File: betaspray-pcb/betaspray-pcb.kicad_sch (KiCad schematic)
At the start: 11 parts, among them SW1 SW_Push, SW2 SW_Push, U1 ESP32-S3-WROOM-1

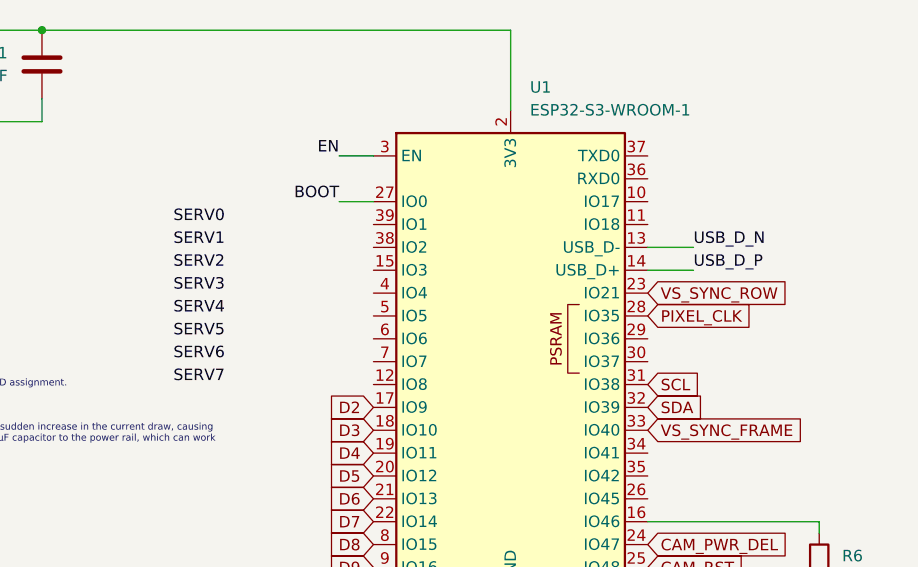
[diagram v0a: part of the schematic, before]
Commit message: fix servo pins
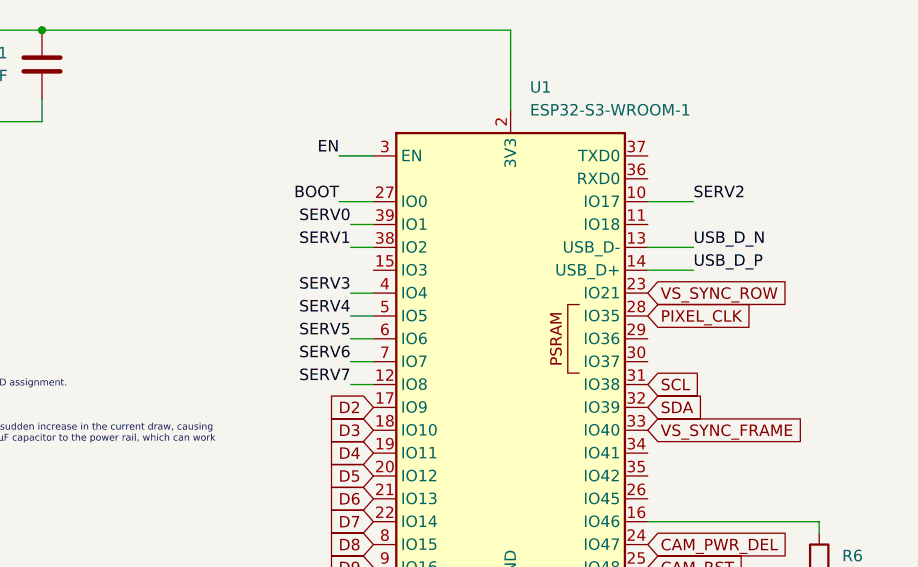
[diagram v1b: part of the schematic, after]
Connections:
- net SERV0: now also U1.39 (IO1)
- net SERV1: now also U1.38 (IO2)
- net SERV2: now also U1.10 (IO17)
- net SERV3: now also U1.4 (IO4)
- net SERV4: now also U1.5 (IO5)
- net SERV5: now also U1.6 (IO6)
- net SERV6: now also U1.7 (IO7)
- net SERV7: now also U1.12 (IO8)
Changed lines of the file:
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@@
+	(wire
+		(pts
+			(xy 93.98 63.5) (xy 96.52 63.5)
+		)
+		(stroke
+			(width 0)
+			(type default)
+		)
+	)
 	(wire
 		(pts
@@
 	(wire
 		(pts
+			(xy 93.98 53.34) (xy 96.52 53.34)
+		)
+		(stroke
+			(width 0)
+			(type default)
+		)
+	)
+	(wire
+		(pts
 			(xy 146.05 92.71) (xy 146.05 93.98)
 		)
@@
 	(wire
 		(pts
+			(xy 93.98 60.96) (xy 96.52 60.96)
+		)
+		(stroke
+			(width 0)
+			(type default)
+		)
+	)
+	(wire
+		(pts
 			(xy 111.76 29.21) (xy 111.76 38.1)
 		)
@@
 	(wire
 		(pts
+			(xy 127 48.26) (xy 132.08 48.26)
+		)
+		(stroke
+			(width 0)
+			(type default)
+		)
+	)
+	(wire
+		(pts
 			(xy 186.69 62.23) (xy 186.69 63.5)
 		)
@@
 	(wire
 		(pts
+			(xy 93.98 68.58) (xy 96.52 68.58)
+		)
+		(stroke
+			(width 0)
+			(type default)
+		)
+	)
+	(wire
+		(pts
 			(xy 146.05 85.09) (xy 146.05 83.82)
 		)
@@
 	(wire
 		(pts
+			(xy 93.98 58.42) (xy 96.52 58.42)
+		)
+		(stroke
+			(width 0)
+			(type default)
+		)
+	)
+	(wire
+		(pts
 			(xy 92.71 48.26) (xy 96.52 48.26)
 		)
@@
 	(wire
 		(pts
+			(xy 93.98 50.8) (xy 96.52 50.8)
+		)
+		(stroke
+			(width 0)
+			(type default)
+		)
+	)
+	(wire
+		(pts
 			(xy 186.69 59.69) (xy 186.69 62.23)
 		)
@@
 		(pts
 			(xy 278.13 11.43) (xy 278.13 82.55)
+		)
+		(stroke
+			(width 0)
+			(type default)
+		)
+	)
+	(wire
+		(pts
+			(xy 93.98 66.04) (xy 96.52 66.04)
 		)
 		(stroke
@@
 	)
 	(label "SERV1"
-		(at 80.01 53.34 180)
+		(at 93.98 53.34 180)
 		(effects
 			(font
@@
 	)
 	(label "SERV0"
-		(at 80.01 50.8 180)
+		(at 93.98 50.8 180)
 		(effects
 			(font
@@
 	)
 	(label "SERV3"
-		(at 80.01 58.42 180)
+		(at 93.98 58.42 180)
 		(effects
 			(font
@@
 	)
 	(label "SERV7"
-		(at 80.01 68.58 180)
+		(at 93.98 68.58 180)
 		(effects
 			(font
@@
 	)
 	(label "SERV6"
-		(at 80.01 66.04 180)
+		(at 93.98 66.04 180)
 		(effects
 			(font
@@
 	)
 	(label "SERV4"
-		(at 80.01 60.96 180)
+		(at 93.98 60.96 180)
 		(effects
 			(font
@@
 	)
 	(label "SERV2"
-		(at 80.01 55.88 180)
-		(effects
-			(font
-				(size 1.27 1.27)
-			)
-			(justify right bottom)
+		(at 132.08 48.26 0)
+		(effects
+			(font
+				(size 1.27 1.27)
+			)
+			(justify left bottom)
 		)
 	)
@@
 	)
 	(label "SERV5"
-		(at 80.01 63.5 180)
-		(effects
-			(font
+		(at 93.98 63.5 180)
+		(effects
+			(font

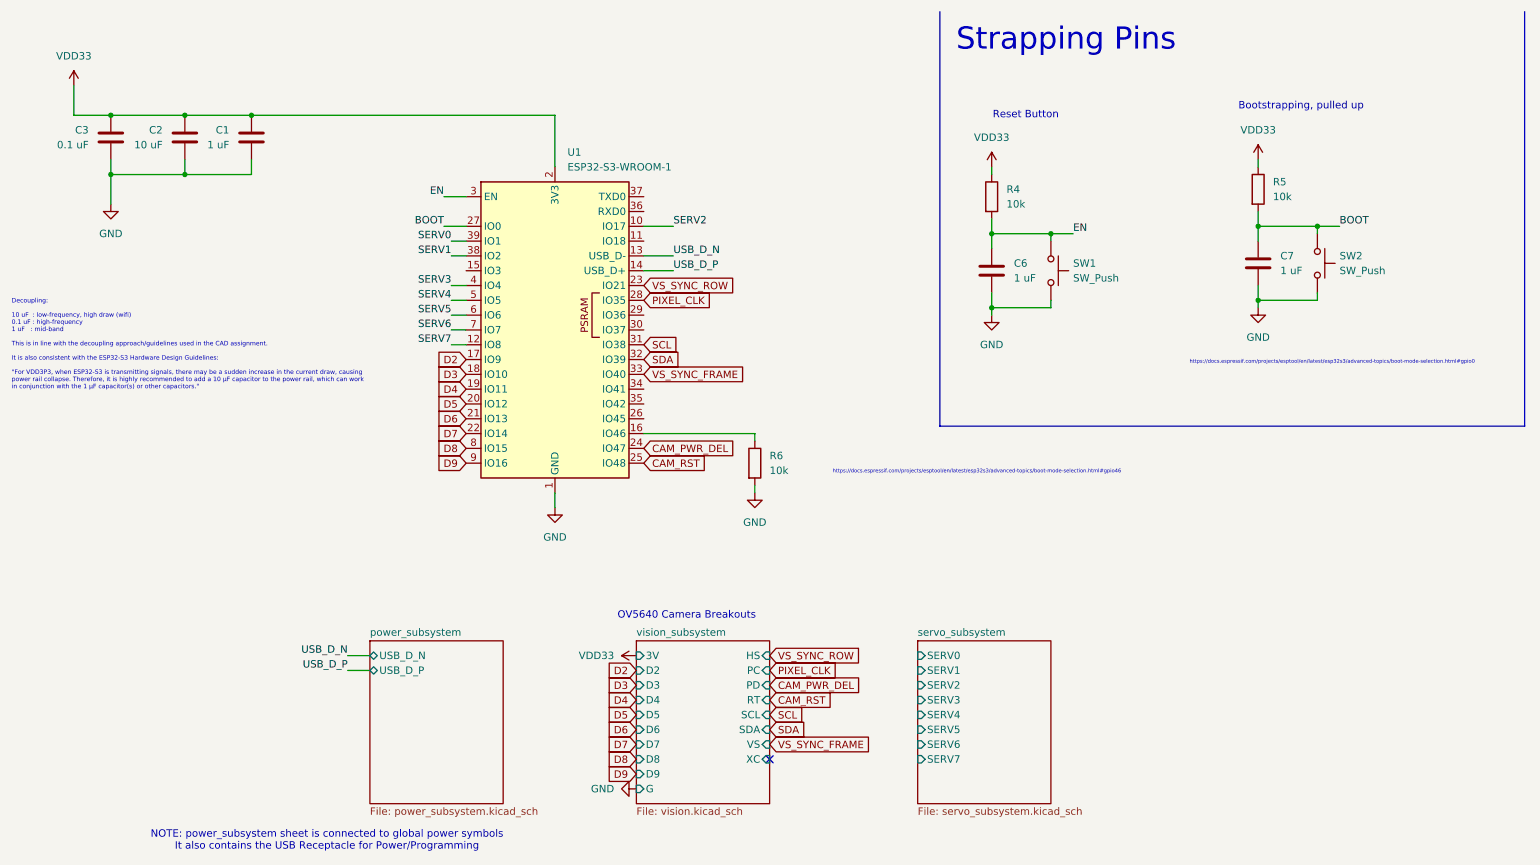
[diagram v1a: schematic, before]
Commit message: Connected Servo labels, added debug led
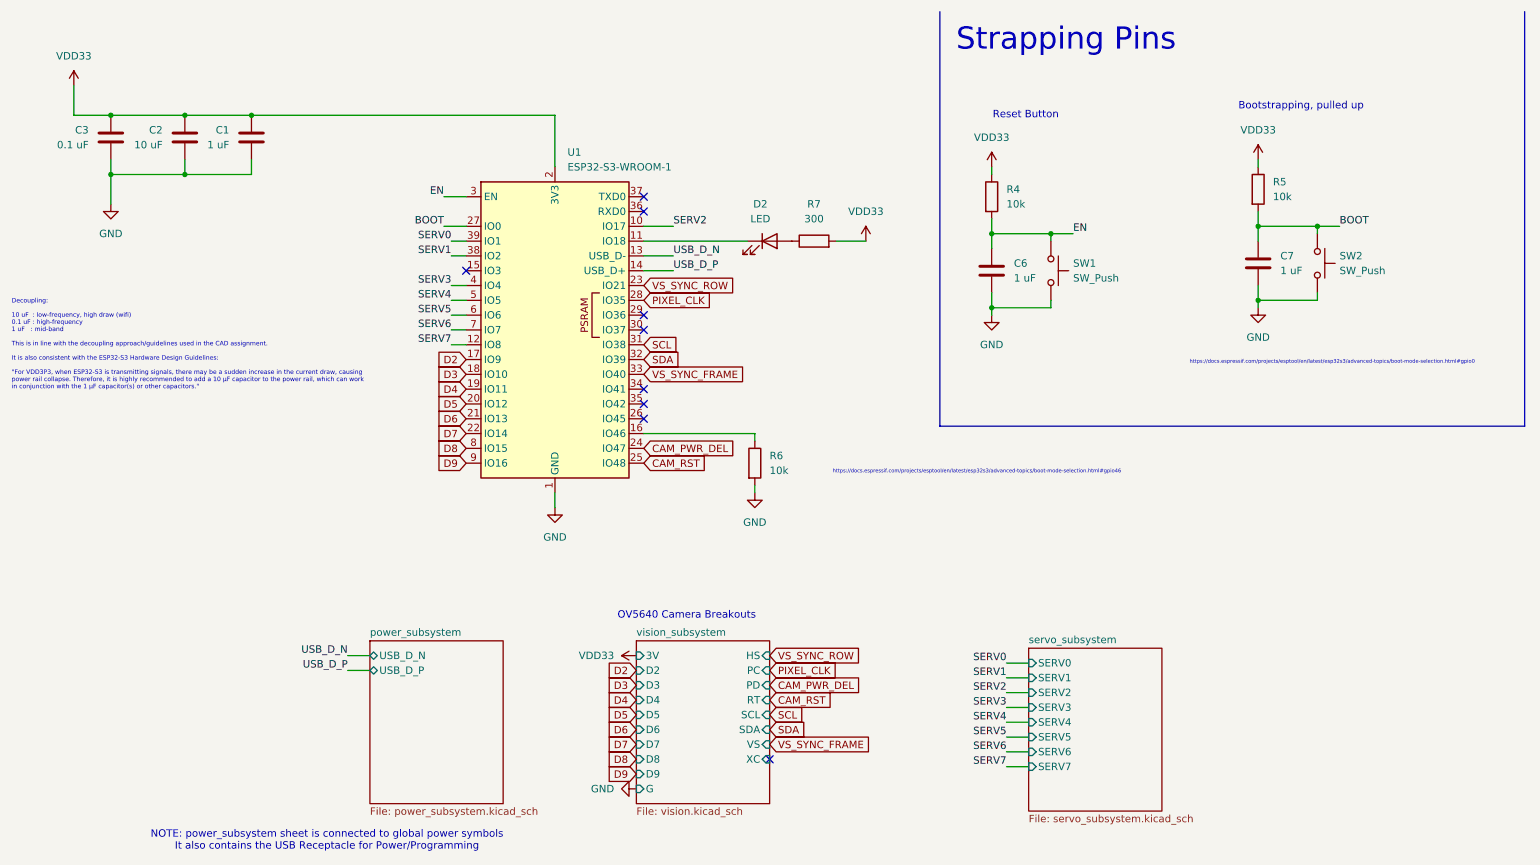
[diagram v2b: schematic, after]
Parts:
- added D2: LED, LED_SMD:LED_0805_2012Metric, symbol betaspray_MCU_Espressif:LED
- added R7: 300, symbol betaspray_MCU_Espressif:R
- C1, C2, C6, C7: symbol betaspray_LDO:C -> betaspray_MCU_Espressif:C
- C3: symbol Device:C -> betaspray_MCU_Espressif:C
- R4, R5, R6: symbol betaspray_LDO:R -> betaspray_MCU_Espressif:R
- SW1, SW2: symbol betaspray_LDO:SW_Push -> betaspray_MCU_Espressif:SW_Push
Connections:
- net VDD33: now also R7.2
- net at U1.11 (IO18): now also D2.1 (K)
- new net: D2.2 (A), R7.1
- no-connect marks 1 -> 9

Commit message: Started layout
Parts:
- C1, C2, C3, C6, C7: footprint (none) -> Capacitor_SMD:C_0805_2012Metric_Pad1.18x1.45mm_HandSolder
- R4, R5, R6, R7: footprint (none) -> Resistor_SMD:R_0805_2012Metric_Pad1.20x1.40mm_HandSolder
- SW1, SW2: footprint (none) -> Button_Switch_THT:SW_PUSH-12mm
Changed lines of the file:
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@@
 			)
 		)
-		(property "Footprint" ""
+		(property "Footprint" "Capacitor_SMD:C_0805_2012Metric_Pad1.18x1.45mm_HandSolder"
 			(at 34.5948 36.83 0)
 			(effects
@@
 			)
 		)
-		(property "Footprint" ""
+		(property "Footprint" "Button_Switch_THT:SW_PUSH-12mm"
 			(at 247.65 54.61 0)
 			(effects
@@
 			)
 		)
-		(property "Footprint" ""
+		(property "Footprint" "Resistor_SMD:R_0805_2012Metric_Pad1.20x1.40mm_HandSolder"
 			(at 156.21 52.578 90)
 			(effects
@@
 			)
 		)
-		(property "Footprint" ""
+		(property "Footprint" "Resistor_SMD:R_0805_2012Metric_Pad1.20x1.40mm_HandSolder"
 			(at 184.912 43.18 90)
 			(effects
@@
 			)
 		)
-		(property "Footprint" ""
+		(property "Footprint" "Capacitor_SMD:C_0805_2012Metric_Pad1.18x1.45mm_HandSolder"
 			(at 187.6552 59.69 0)
 			(effects
@@
 			)
 		)
-		(property "Footprint" ""
+		(property "Footprint" "Button_Switch_THT:SW_PUSH-12mm"
 			(at 201.93 55.88 0)
 			(effects
@@
 			)
 		)
-		(property "Footprint" ""
+		(property "Footprint" "Capacitor_SMD:C_0805_2012Metric_Pad1.18x1.45mm_HandSolder"
 			(at 233.3752 58.42 0)
 			(effects
@@
 			)
 		)
-		(property "Footprint" ""
+		(property "Footprint" "Resistor_SMD:R_0805_2012Metric_Pad1.20x1.40mm_HandSolder"
 			(at 144.272 88.9 90)
 			(effects
@@
 			)
 		)
-		(property "Footprint" ""
+		(property "Footprint" "Resistor_SMD:R_0805_2012Metric_Pad1.20x1.40mm_HandSolder"
 			(at 230.632 41.91 90)
 			(effects
@@
 			)
 		)
-		(property "Footprint" ""
+		(property "Footprint" "Capacitor_SMD:C_0805_2012Metric_Pad1.18x1.45mm_HandSolder"
 			(at 47.2948 36.83 0)
 			(effects
@@
 			)
 		)
-		(property "Footprint" ""
+		(property "Footprint" "Capacitor_SMD:C_0805_2012Metric_Pad1.18x1.45mm_HandSolder"
 			(at 58.7248 36.83 0)
 			(effects

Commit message: Trying to route
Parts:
- SW1, SW2: footprint Button_Switch_THT:SW_PUSH-12mm -> Button_Switch_SMD:SW_DIP_SPSTx02_Slide_9.78x7.26mm_W8.61mm_P2.54mm
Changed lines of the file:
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@@
 			)
 		)
-		(property "Footprint" "Button_Switch_THT:SW_PUSH-12mm"
+		(property "Footprint" "Button_Switch_SMD:SW_DIP_SPSTx02_Slide_9.78x7.26mm_W8.61mm_P2.54mm"
 			(at 247.65 54.61 0)
 			(effects
@@
 			)
 		)
-		(property "Footprint" "Button_Switch_THT:SW_PUSH-12mm"
+		(property "Footprint" "Button_Switch_SMD:SW_DIP_SPSTx02_Slide_9.78x7.26mm_W8.61mm_P2.54mm"
 			(at 201.93 55.88 0)
 			(effects

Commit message: Trying to route
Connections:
- net CAM_PWR_DEL: now also U1.28 (IO35); no longer U1.24 (IO47)
- net D2: now also U1.24 (IO47); no longer U1.17 (IO9)
- net D3: now also U1.23 (IO21); no longer U1.18 (IO10)
- net PIXEL_CLK: now also U1.39 (IO1); no longer U1.28 (IO35)
- net SCL: now also U1.33 (IO40); no longer U1.31 (IO38)
- net SERV0: now also U1.4 (IO4); no longer U1.39 (IO1)
- net SERV1: now also U1.5 (IO5); no longer U1.38 (IO2)
- net SERV3: now also U1.17 (IO9); no longer U1.4 (IO4)
- net SERV4: now also U1.6 (IO6); no longer U1.5 (IO5)
- net SERV5: now also U1.12 (IO8); no longer U1.6 (IO6)
- net SERV7: now also U1.18 (IO10); no longer U1.12 (IO8)
- net VS_SYNC_FRAME: now also U1.31 (IO38); no longer U1.33 (IO40)
- net VS_SYNC_ROW: now also U1.38 (IO2); no longer U1.23 (IO21)
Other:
- sheet power_subsystem ports: added VDD3V; removed none

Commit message: Routed
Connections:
- net CAM_PWR_DEL: now also U1.19 (IO11); no longer U1.28 (IO35)
- net CAM_RST: now also U1.26 (IO45); no longer U1.25 (IO48)
- net D2: now also U1.20 (IO12); no longer U1.24 (IO47)
- net D3: now also U1.31 (IO38); no longer U1.23 (IO21)
- net D4: now also U1.21 (IO13); no longer U1.19 (IO11)
- net D5: now also U1.32 (IO39); no longer U1.20 (IO12)
- net D6: now also U1.22 (IO14); no longer U1.21 (IO13)
- net D7: now also U1.33 (IO40); no longer U1.22 (IO14)
- net D8: now also U1.23 (IO21); no longer U1.8 (IO15)
- net D9: now also U1.34 (IO41); no longer U1.9 (IO16)
- net PIXEL_CLK: now also U1.35 (IO42); no longer U1.39 (IO1)
- net SCL: now also U1.39 (IO1); no longer U1.33 (IO40)
- net SDA: now also U1.25 (IO48); no longer U1.32 (IO39)
- net SERV1: now also U1.6 (IO6); no longer U1.5 (IO5)
- net SERV2: now also U1.11 (IO18); no longer U1.10 (IO17)
- net SERV3: now also U1.12 (IO8); no longer U1.17 (IO9)
- net SERV4: now also U1.17 (IO9); no longer U1.6 (IO6)
- net SERV5: now also U1.5 (IO5); no longer U1.12 (IO8)
- net VS_SYNC_FRAME: now also U1.38 (IO2); no longer U1.31 (IO38)
- net VS_SYNC_ROW: now also U1.24 (IO47); no longer U1.38 (IO2)
- net at D2.1 (K): now also U1.10 (IO17); no longer U1.11 (IO18)
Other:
- moved on the sheet: D2, R7

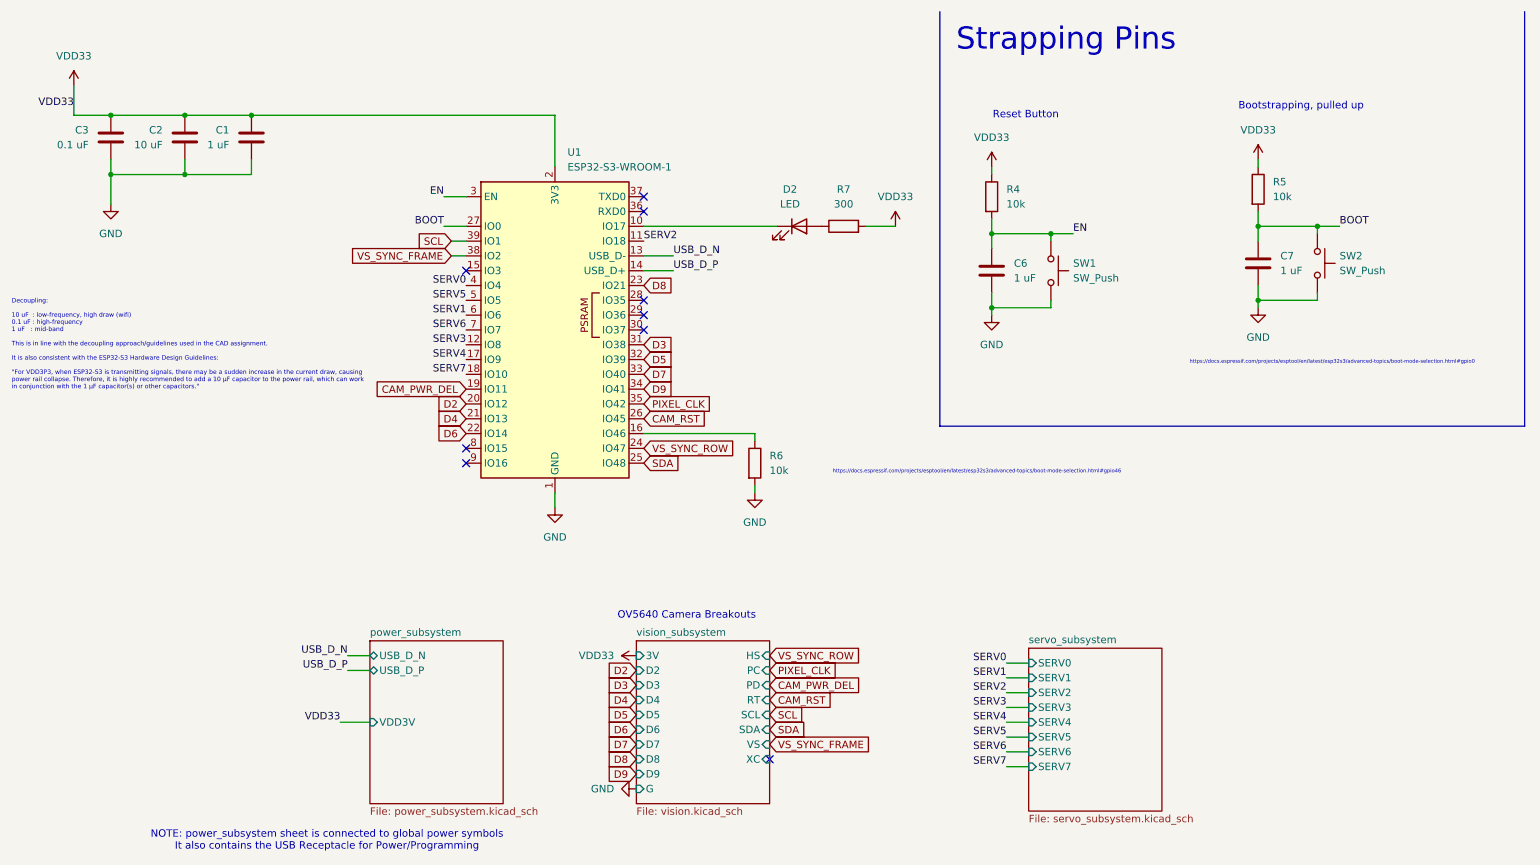
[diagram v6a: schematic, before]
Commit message: Added lasers to schematic and footprint
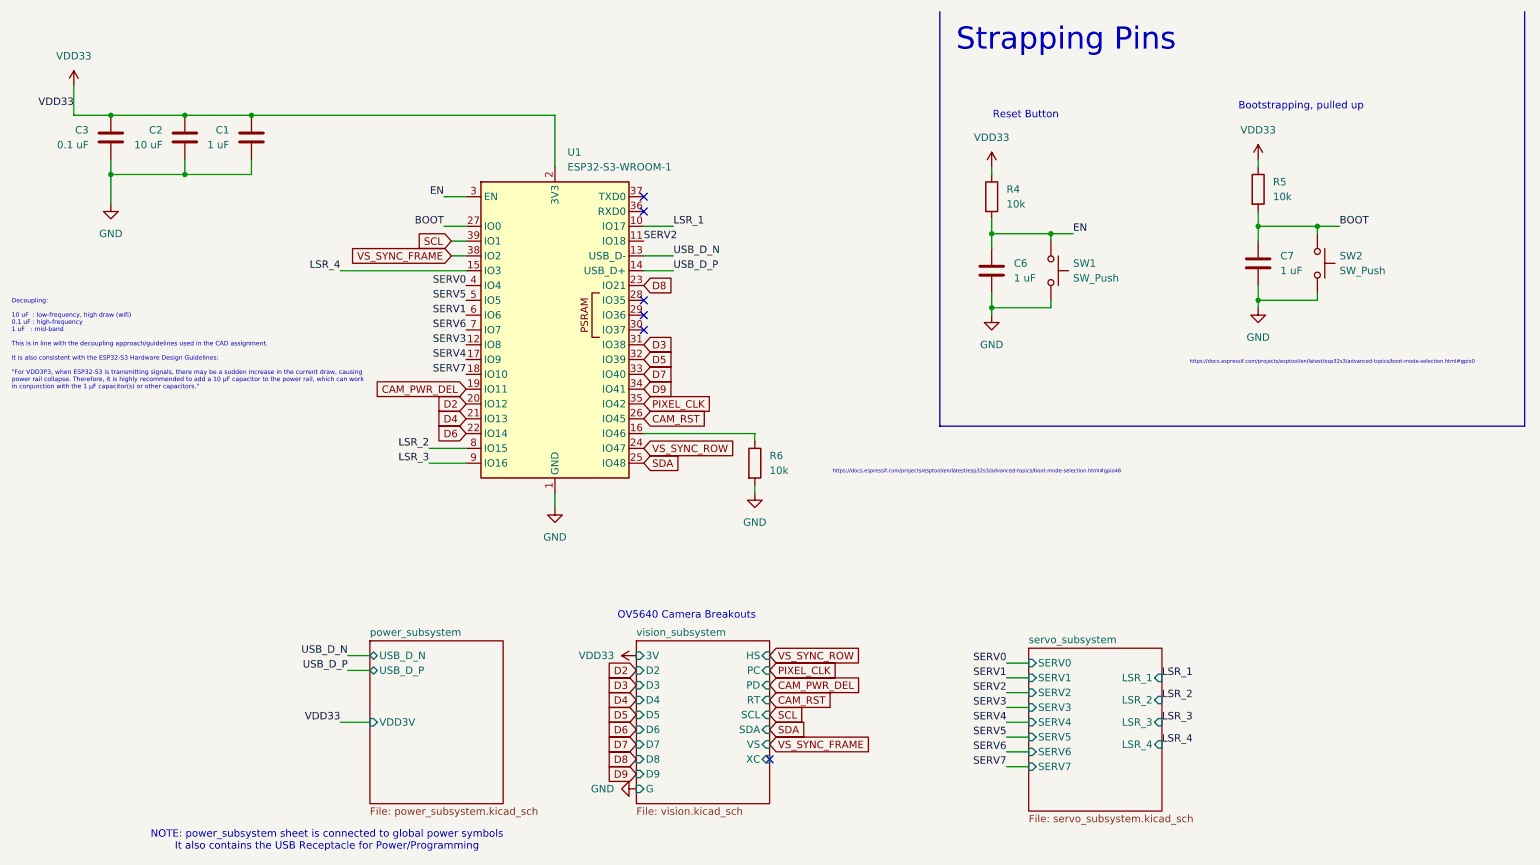
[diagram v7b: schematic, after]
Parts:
- removed D2: LED, LED_SMD:LED_0805_2012Metric, symbol betaspray_MCU_Espressif:LED
- removed R7: 300, Resistor_SMD:R_0805_2012Metric_Pad1.20x1.40mm_HandSolder, symbol betaspray_MCU_Espressif:R
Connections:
- net LSR_1: now reaches U1.10 (IO17)
- net LSR_4: now reaches U1.15 (IO3)
- net LSR_2: now reaches U1.8 (IO15)
- net LSR_3: now reaches U1.9 (IO16)
- no-connect marks 9 -> 6
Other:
- sheet servo_subsystem ports: added LSR_1, LSR_2, LSR_3, LSR_4; removed none
